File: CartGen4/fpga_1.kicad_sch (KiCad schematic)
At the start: 5 parts, among them U9 LFXP2-8E-5MN132C

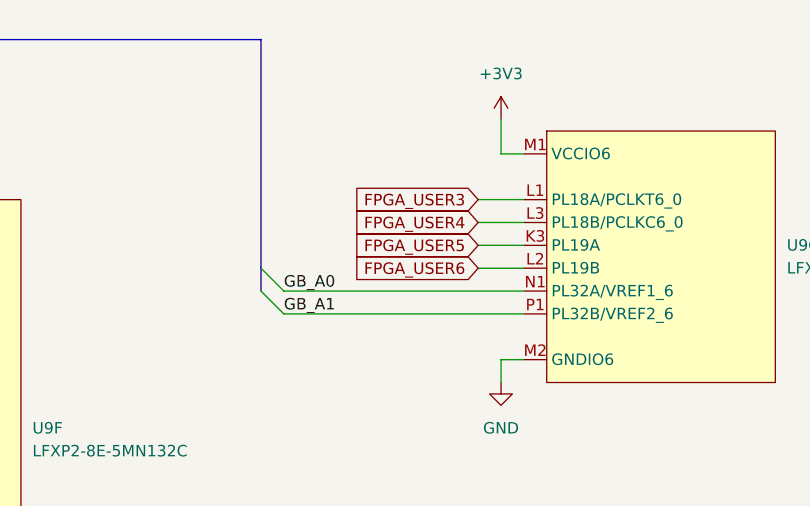
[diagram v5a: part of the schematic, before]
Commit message: Routed expansion port
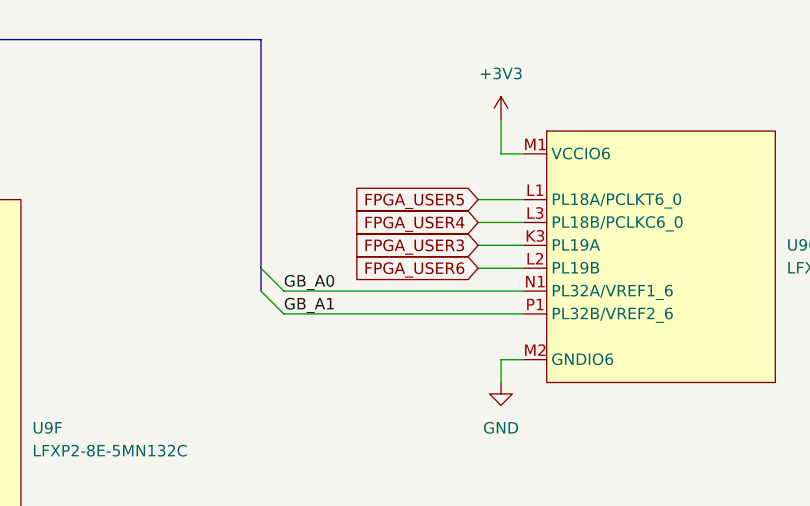
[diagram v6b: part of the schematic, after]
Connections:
- net FPGA_USER3: now also U9.K3 (PL19A); no longer U9.L1 (PL18A/PCLKT6_0)
- net FPGA_USER5: now also U9.L1 (PL18A/PCLKT6_0); no longer U9.K3 (PL19A)
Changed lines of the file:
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@@
     )
   )
-  (global_label "FPGA_USER5" (shape input) (at 220.98 62.23 180) (fields_autoplaced)
+  (global_label "FPGA_USER3" (shape input) (at 220.98 62.23 180) (fields_autoplaced)
     (effects (font (size 1.27 1.27)) (justify right))
     (property "Intersheet References" "${INTERSHEET_REFS}" (id 0) (at 206.7136 62.1506 0)
+      (effects (font (size 1.27 1.27)) (justify right) hide)
+    )
+  )
+  (global_label "FPGA_USER5" (shape input) (at 220.98 57.15 180) (fields_autoplaced)
+    (effects (font (size 1.27 1.27)) (justify right))
+    (property "Intersheet References" "${INTERSHEET_REFS}" (id 0) (at 206.7136 57.0706 0)
       (effects (font (size 1.27 1.27)) (justify right) hide)
     )
@@
       (effects (font (size 1.27 1.27)) (justify right) hide)
     )
-  )
-  (global_label "FPGA_USER3" (shape input) (at 220.98 57.15 180) (fields_autoplaced)
-    (effects (font (size 1.27 1.27)) (justify right))
-    (property "Intersheet References" "${INTERSHEET_REFS}" (id 0) (at 206.7136 57.0706 0)
-      (effects (font (size 1.27 1.27)) (justify right) hide)
-    )

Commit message: Minor adjustments
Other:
- note added: "This sheet contains connections to the FPGA. It contains the following: - Gameboy connections (address, data and control) - Some RAM signals - Some general purpose signals"
- note removed: "This sheet contains connections to the FPGA. It contains the following: - Gameboy connections (address, data and control)"
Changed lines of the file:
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@@
     (stroke (width 0) (type default) (color 0 0 0 0))
   )
-  (text "This sheet contains connections to the FPGA.\nIt contains the following:\n    - Gameboy connections (address, data and control)"
-    (at 179.07 173.99 0)
+  (text "This sheet contains connections to the FPGA.\nIt contains the following:\n    - Gameboy connections (address, data and control)\n    - Some RAM signals\n    - Some general purpose signals"
+    (at 179.07 177.8 0)
     (effects (font (size 1.27 1.27)) (justify left bottom))
   )

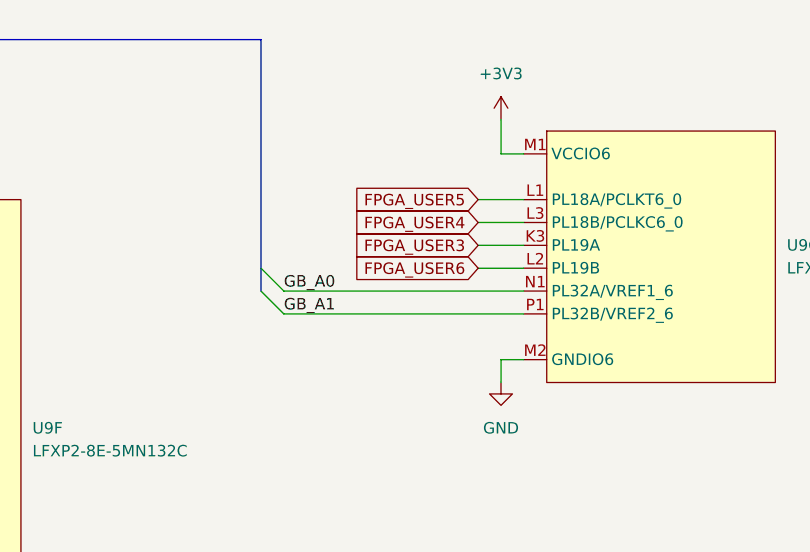
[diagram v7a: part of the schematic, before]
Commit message: Fixed GB_BUS_EN not being on 3V3 bank Added CLK_EN to ext clock
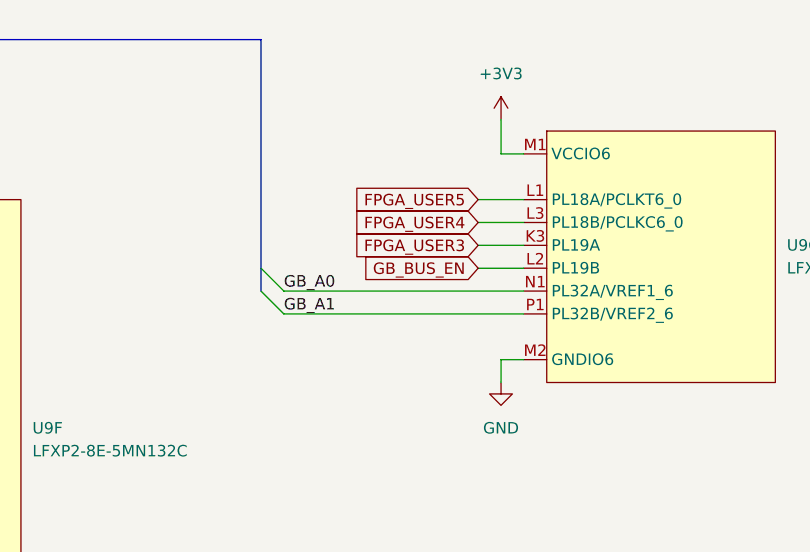
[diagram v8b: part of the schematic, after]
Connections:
- net FPGA_USER6 renamed GB_BUS_EN
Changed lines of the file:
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@@
     )
   )
-  (global_label "FPGA_USER6" (shape input) (at 220.98 64.77 180) (fields_autoplaced)
+  (global_label "GB_BUS_EN" (shape input) (at 220.98 64.77 180) (fields_autoplaced)
     (effects (font (size 1.27 1.27)) (justify right))
-    (property "Intersheet References" "${INTERSHEET_REFS}" (id 0) (at 206.7136 64.6906 0)
+    (property "Intersheet References" "${INTERSHEET_REFS}" (id 0) (at 207.8021 64.6906 0)
       (effects (font (size 1.27 1.27)) (justify right) hide)
     )
